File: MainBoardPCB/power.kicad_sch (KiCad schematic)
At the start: 4 parts, among them U5 NCP718xSN250

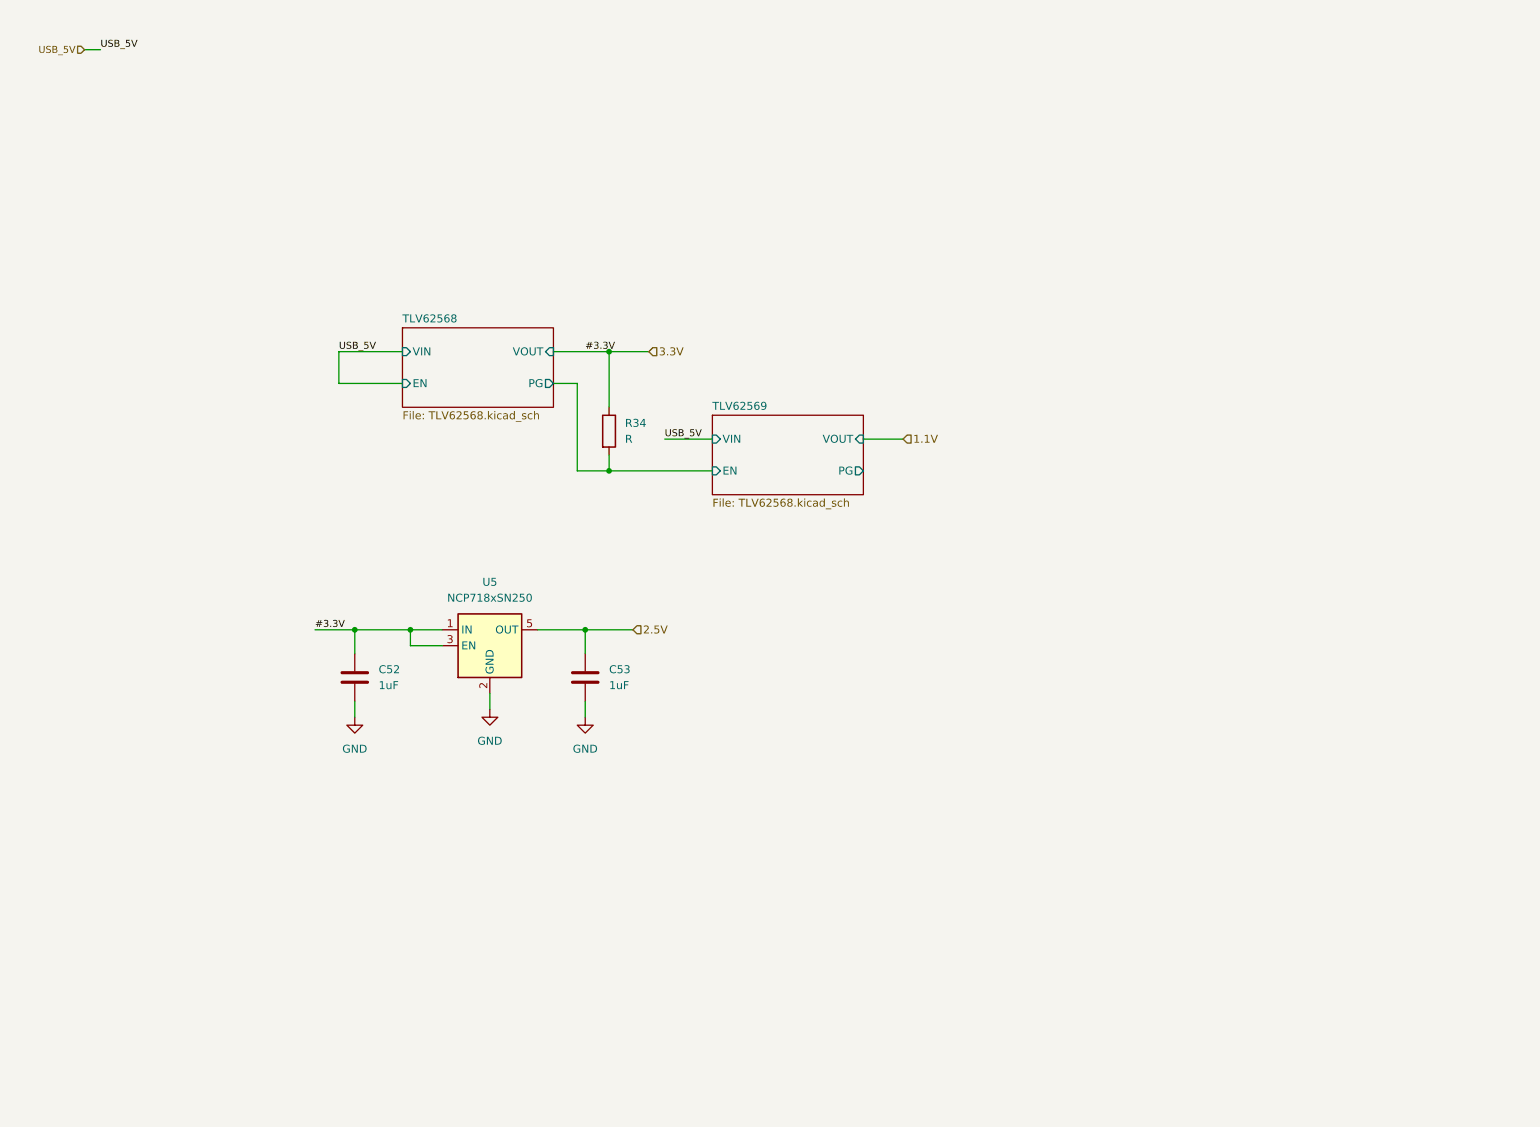
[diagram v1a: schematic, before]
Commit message: New Fusion main board version using a more beefy MCU.
Signed-off-by: Alexis Jeandet <alexis.jeandet@member.fsf.org>
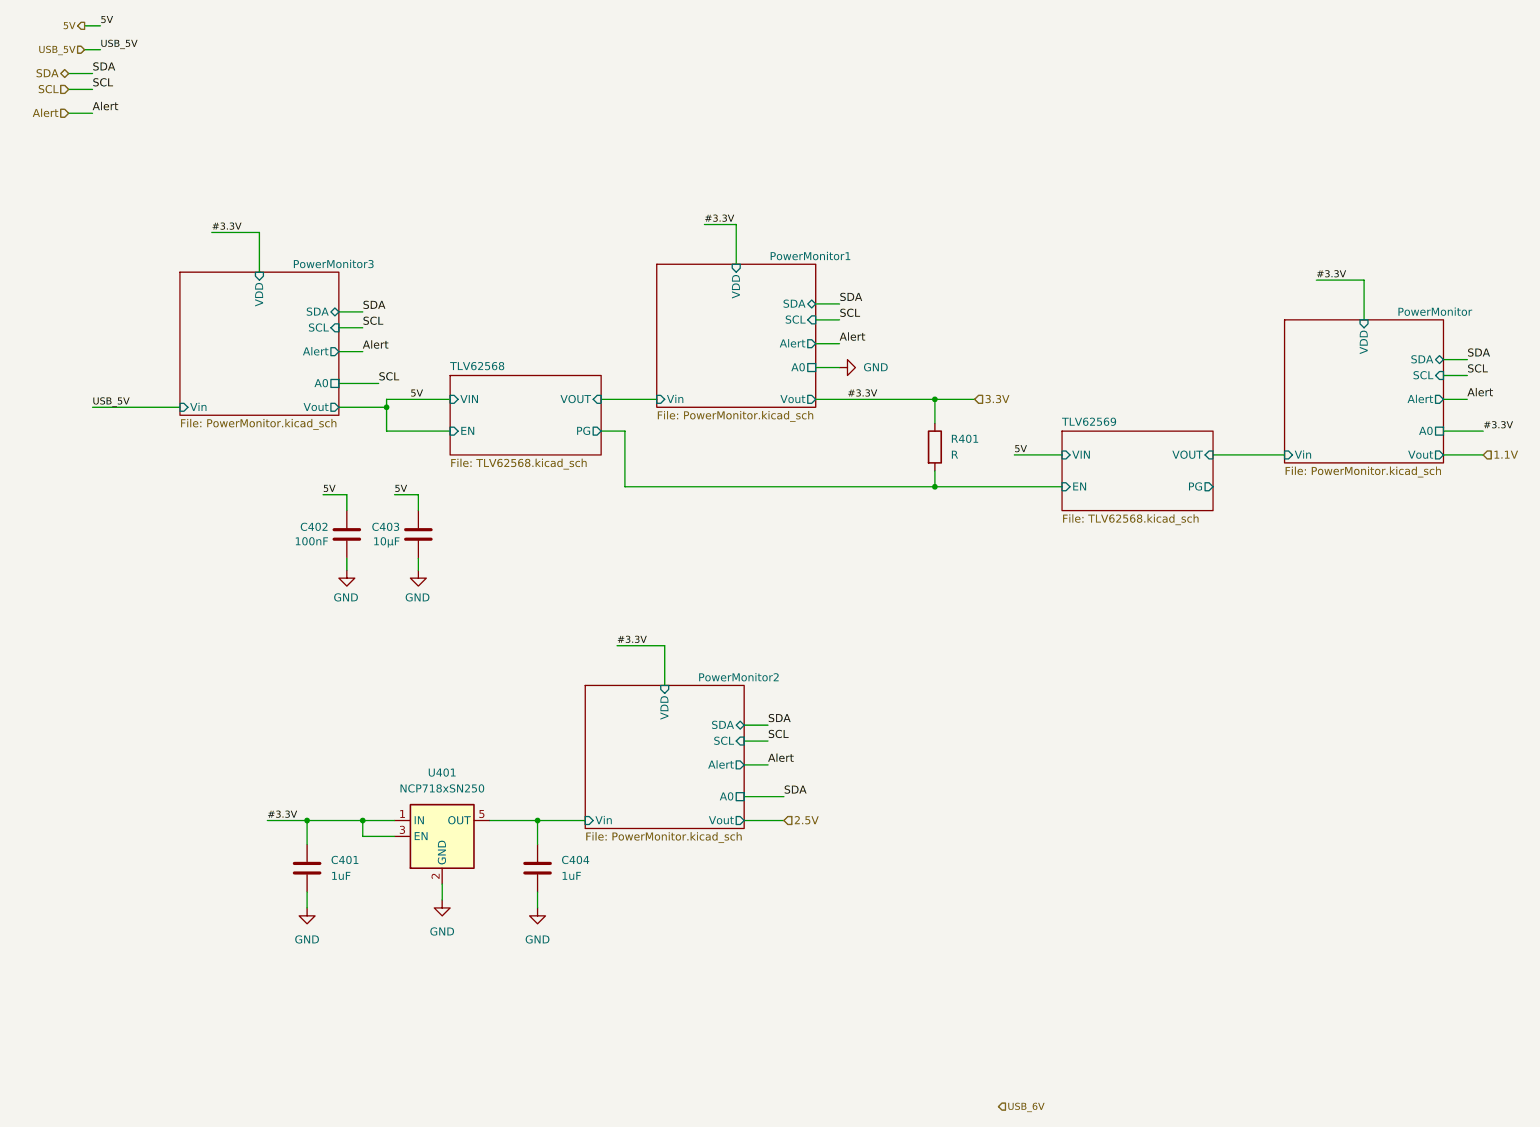
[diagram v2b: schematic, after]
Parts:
- added C402: 100nF, Capacitor_SMD:C_0402_1005Metric, symbol Device:C
- added C403: 10µF, Capacitor_SMD:C_1206_3216Metric_Pad1.33x1.80mm_HandSolder, symbol Device:C
- renumbered C52 to C401, C53 to C404, R34 to R401, U5 to U401
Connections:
- net 2.5V: no longer C404.1, U401.5 (OUT)
- net GND: now also C402.2, C403.2
- new net 5V: C402.1, C403.1
- new net PowerMonitor2/Vin: C404.1, U401.5 (OUT)
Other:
- added sheet PowerMonitor (PowerMonitor.kicad_sch)
- added sheet PowerMonitor1 (PowerMonitor.kicad_sch)
- added sheet PowerMonitor2 (PowerMonitor.kicad_sch)
- added sheet PowerMonitor3 (PowerMonitor.kicad_sch)
- moved on the sheet: C401, C404, R401, U401

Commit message: New FPGA only version
Signed-off-by: Alexis Jeandet <alexis.jeandet@member.fsf.org>
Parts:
- C401, C404: footprint Capacitor_SMD:C_0603_1608Metric_Pad1.08x0.95mm_HandSolder -> Capacitor_SMD:C_0805_2012Metric_Pad1.18x1.45mm_HandSolder
- C402: footprint Capacitor_SMD:C_0402_1005Metric -> Capacitor_SMD:C_0402_1005Metric_Pad0.74x0.62mm_HandSolder
- R401: value R -> 100k
